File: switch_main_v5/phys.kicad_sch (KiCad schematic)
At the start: 0 parts

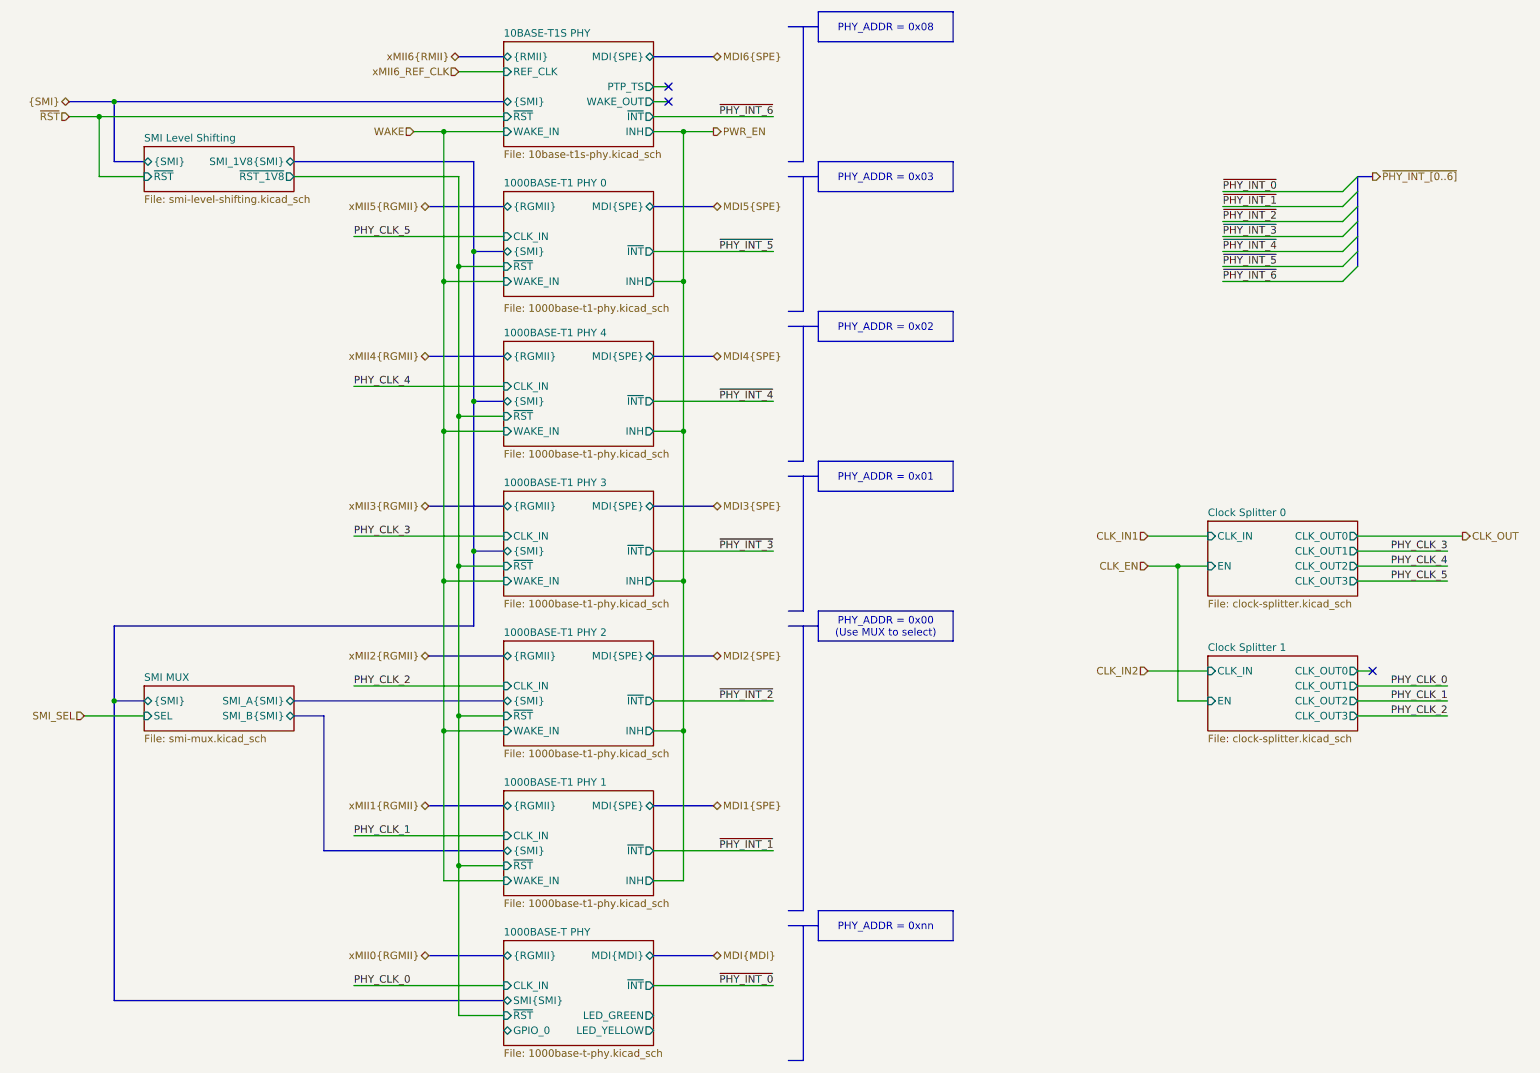
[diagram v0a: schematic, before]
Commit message: MDIO multiplexing
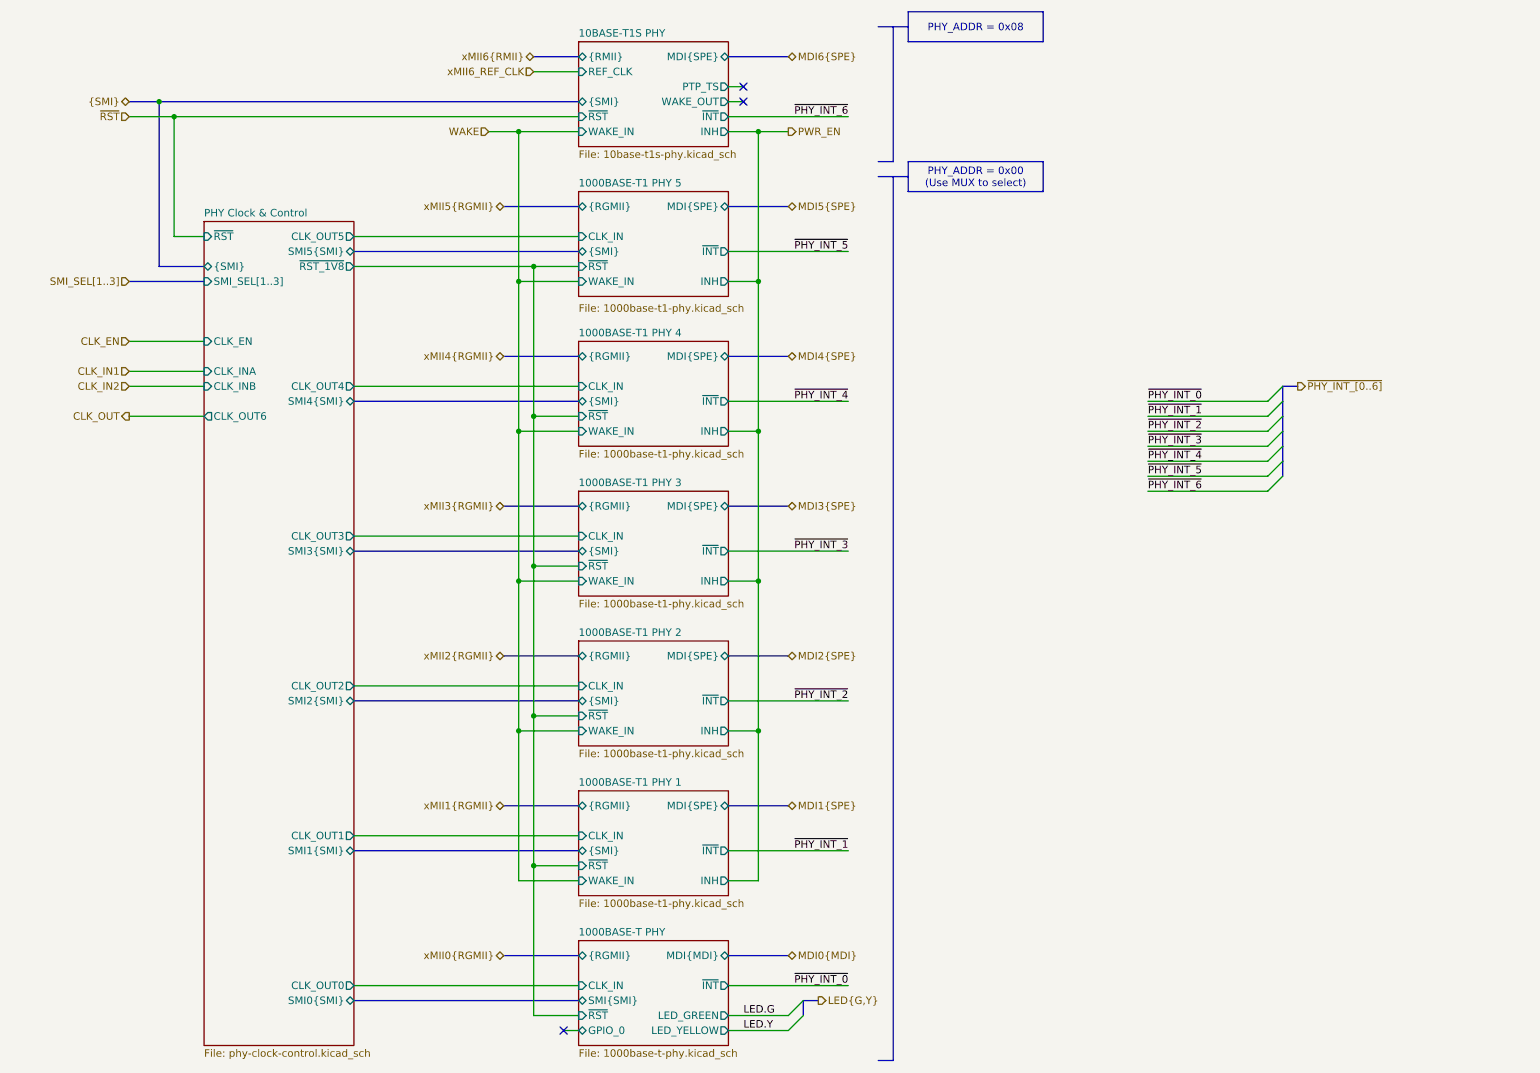
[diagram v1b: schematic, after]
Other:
- sheet 1000BASE-T1 PHY 0 renamed 1000BASE-T1 PHY 5
- sheet SMI Level Shifting renamed PHY Clock & Control
- removed sheet Clock Splitter 0
- removed sheet Clock Splitter 1
- removed sheet SMI MUX
- sheet PHY Clock & Control: file smi-level-shifting.kicad_sch -> phy-clock-control.kicad_sch
- sheet PHY Clock & Control ports: added CLK_EN, CLK_INA, CLK_INB, CLK_OUT0, CLK_OUT1, CLK_OUT2, CLK_OUT3, CLK_OUT4, CLK_OUT5, CLK_OUT6, SMI0{SMI}, SMI1{SMI}, SMI2{SMI}, SMI3{SMI}, SMI4{SMI}, SMI5{SMI}, SMI_SEL[1..3]; removed SMI_1V8{SMI}

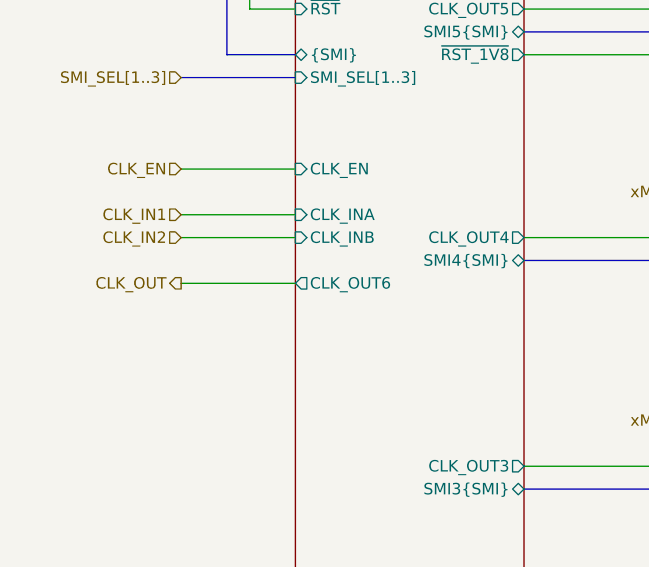
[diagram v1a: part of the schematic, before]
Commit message: Changed main 3V3 regulator to 3A, added switch 2 crystal & other changes
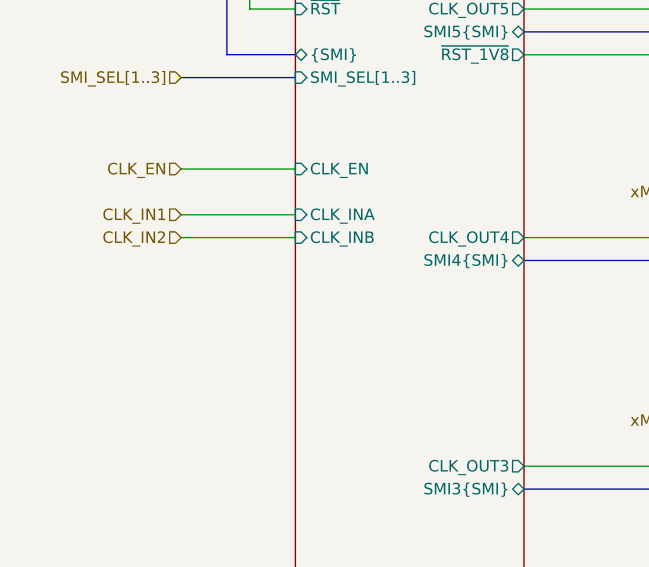
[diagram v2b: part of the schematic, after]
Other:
- sheet PHY Clock & Control ports: added none; removed CLK_OUT6
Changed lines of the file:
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@@
-		)
-	)
-	(wire
-		(pts
-			(xy 33.02 83.82) (xy 45.72 83.82)
-		)
-		(stroke
-			(width 0)
-			(type default)
 		)
 	)
@@
 		(shape input)
 		(at 101.6 25.4 180)
-		(effects
-			(font
-				(size 1.27 1.27)
-			)
-			(justify right)
-		)
-	)
-	(hierarchical_label "CLK_OUT"
-		(shape output)
-		(at 33.02 83.82 180)
 		(effects
 			(font
@@
 			)
 		)
-		(pin "CLK_OUT6" output
-			(at 45.72 83.82 180)
-			(effects
-				(font
-					(size 1.27 1.27)
-				)
-				(justify left)
-			)
-		)

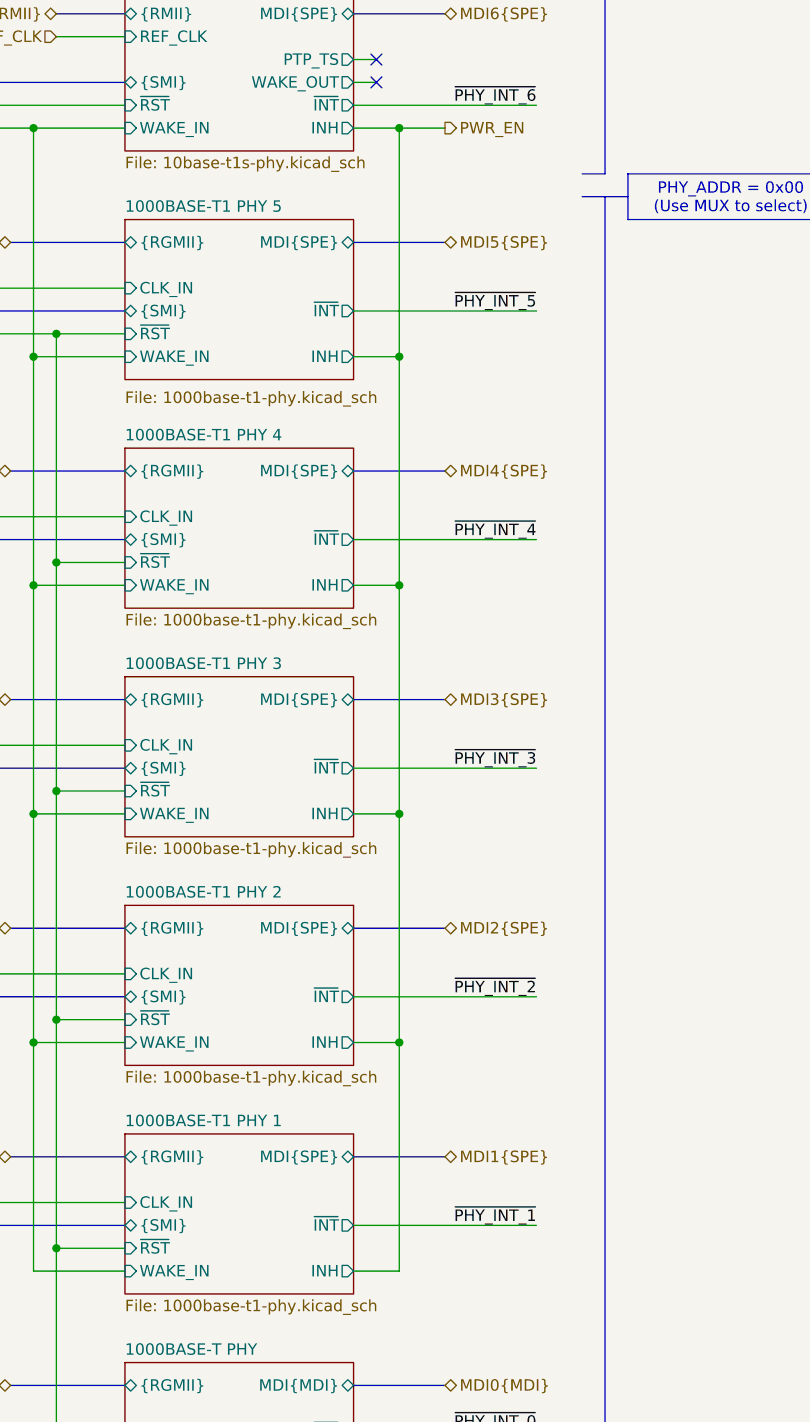
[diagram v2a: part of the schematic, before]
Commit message: PHY3 RGMII routed and length matched
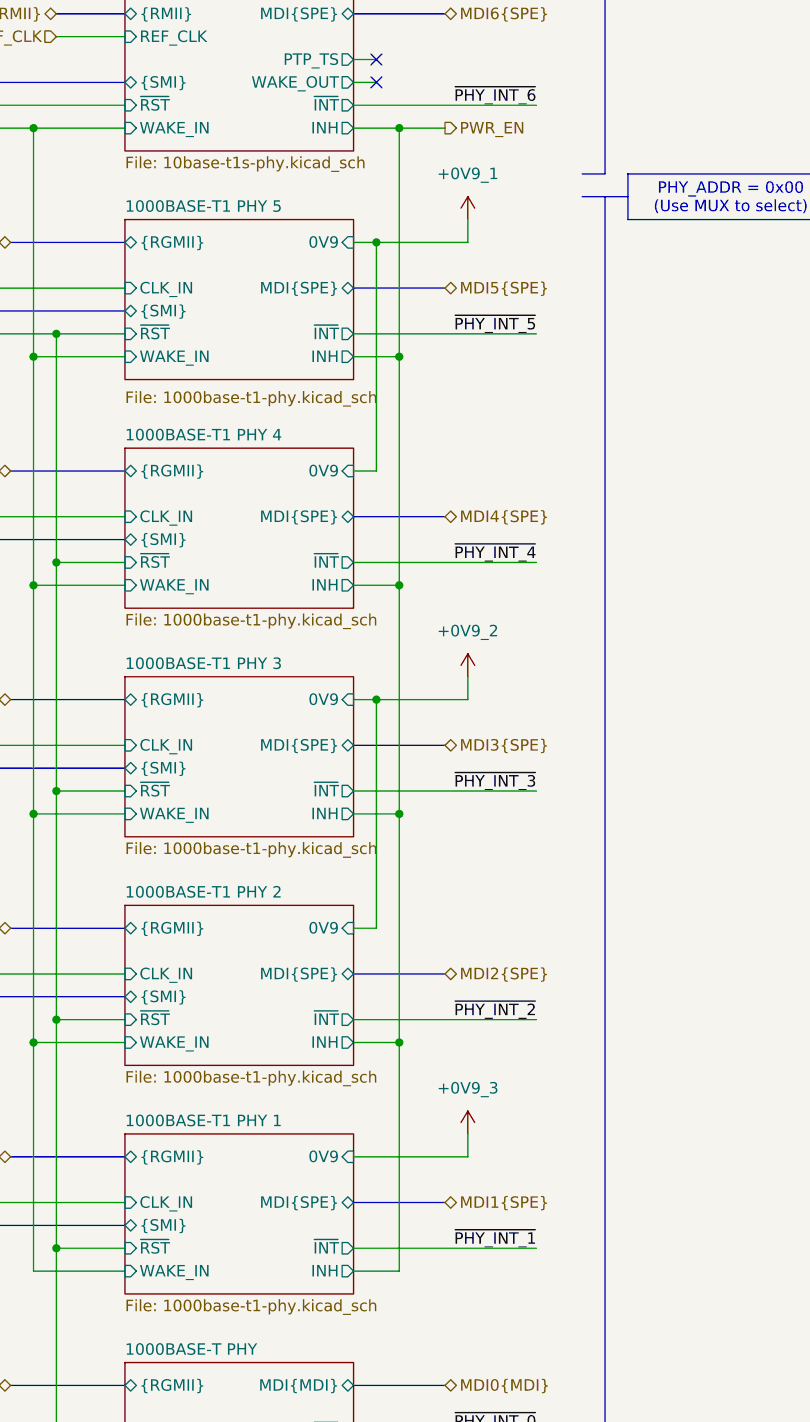
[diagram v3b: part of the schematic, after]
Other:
- sheet 1000BASE-T1 PHY 1 ports: added 0V9; removed none
- sheet 1000BASE-T1 PHY 2 ports: added 0V9; removed none
- sheet 1000BASE-T1 PHY 3 ports: added 0V9; removed none
- sheet 1000BASE-T1 PHY 4 ports: added 0V9; removed none
- sheet 1000BASE-T1 PHY 5 ports: added 0V9; removed none

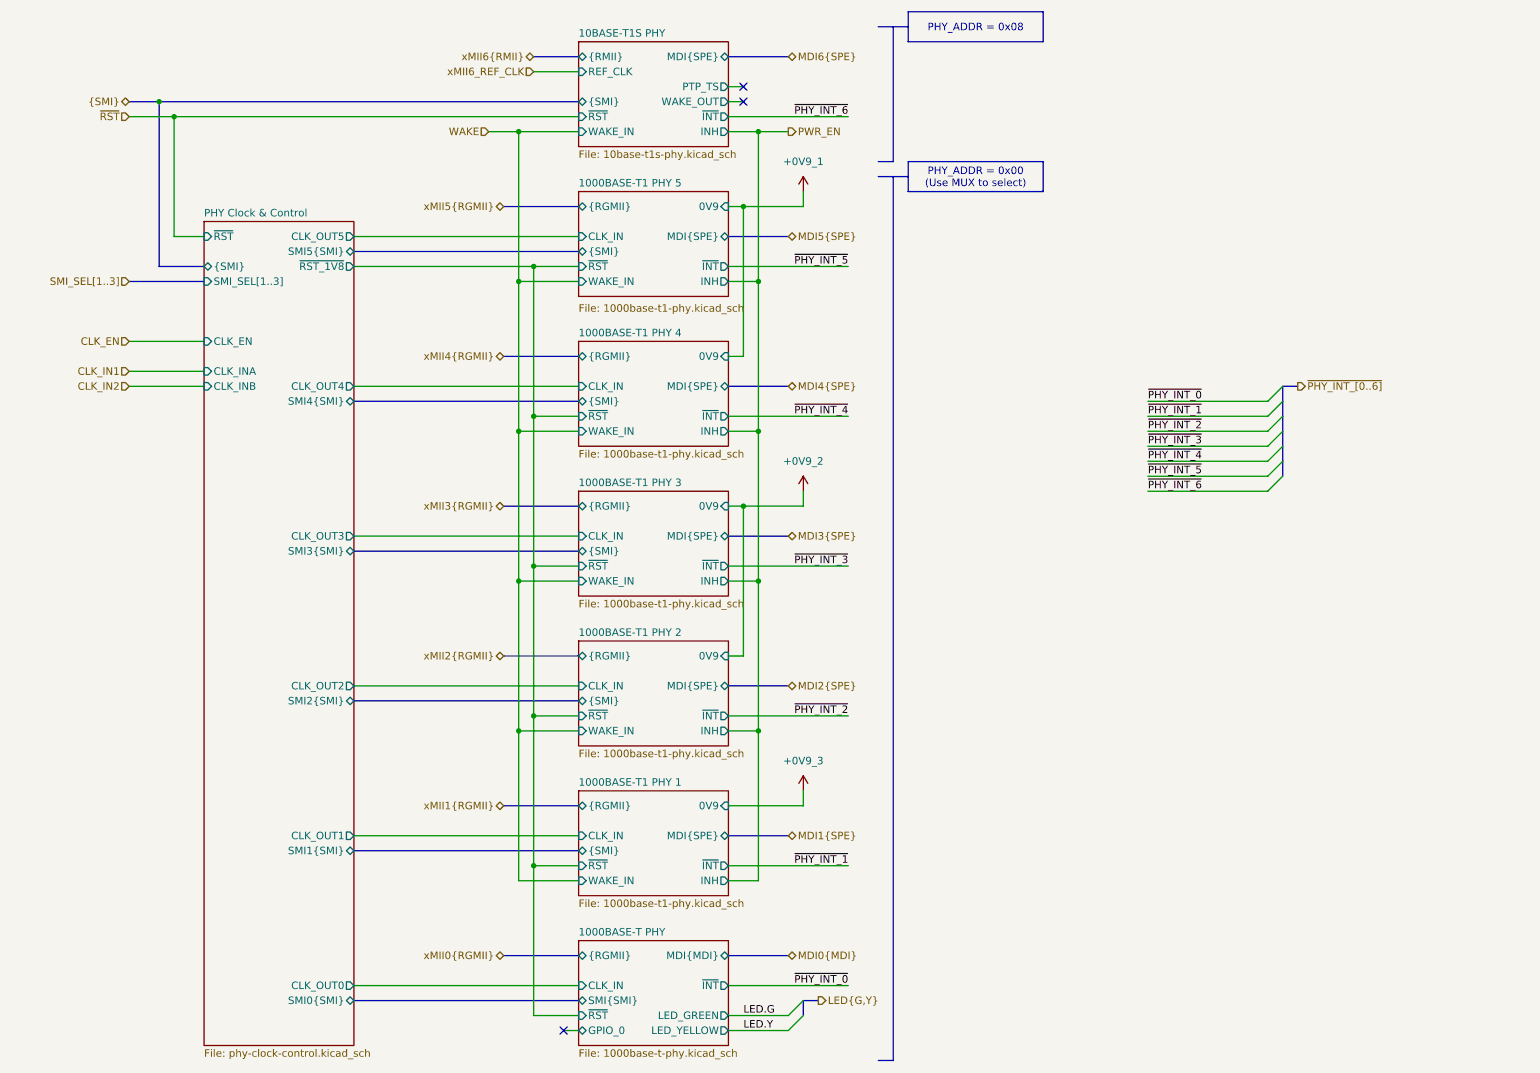
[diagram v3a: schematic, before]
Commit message: Fixed test points
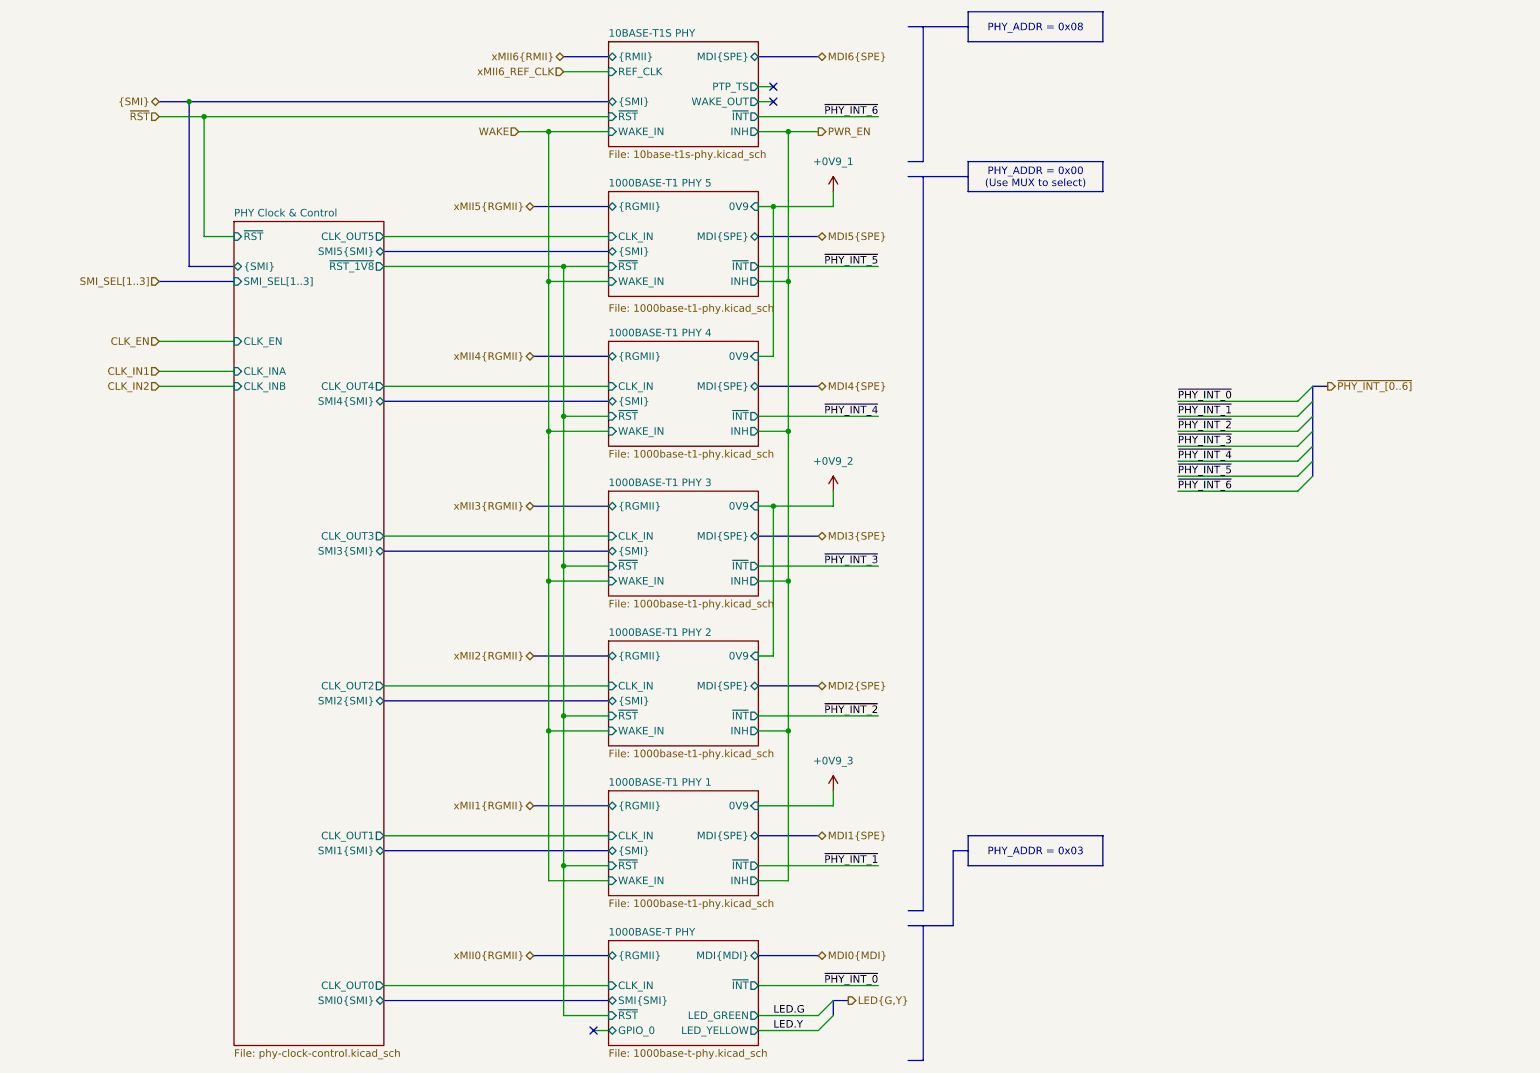
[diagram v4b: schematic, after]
